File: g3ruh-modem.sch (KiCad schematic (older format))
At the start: 0 parts

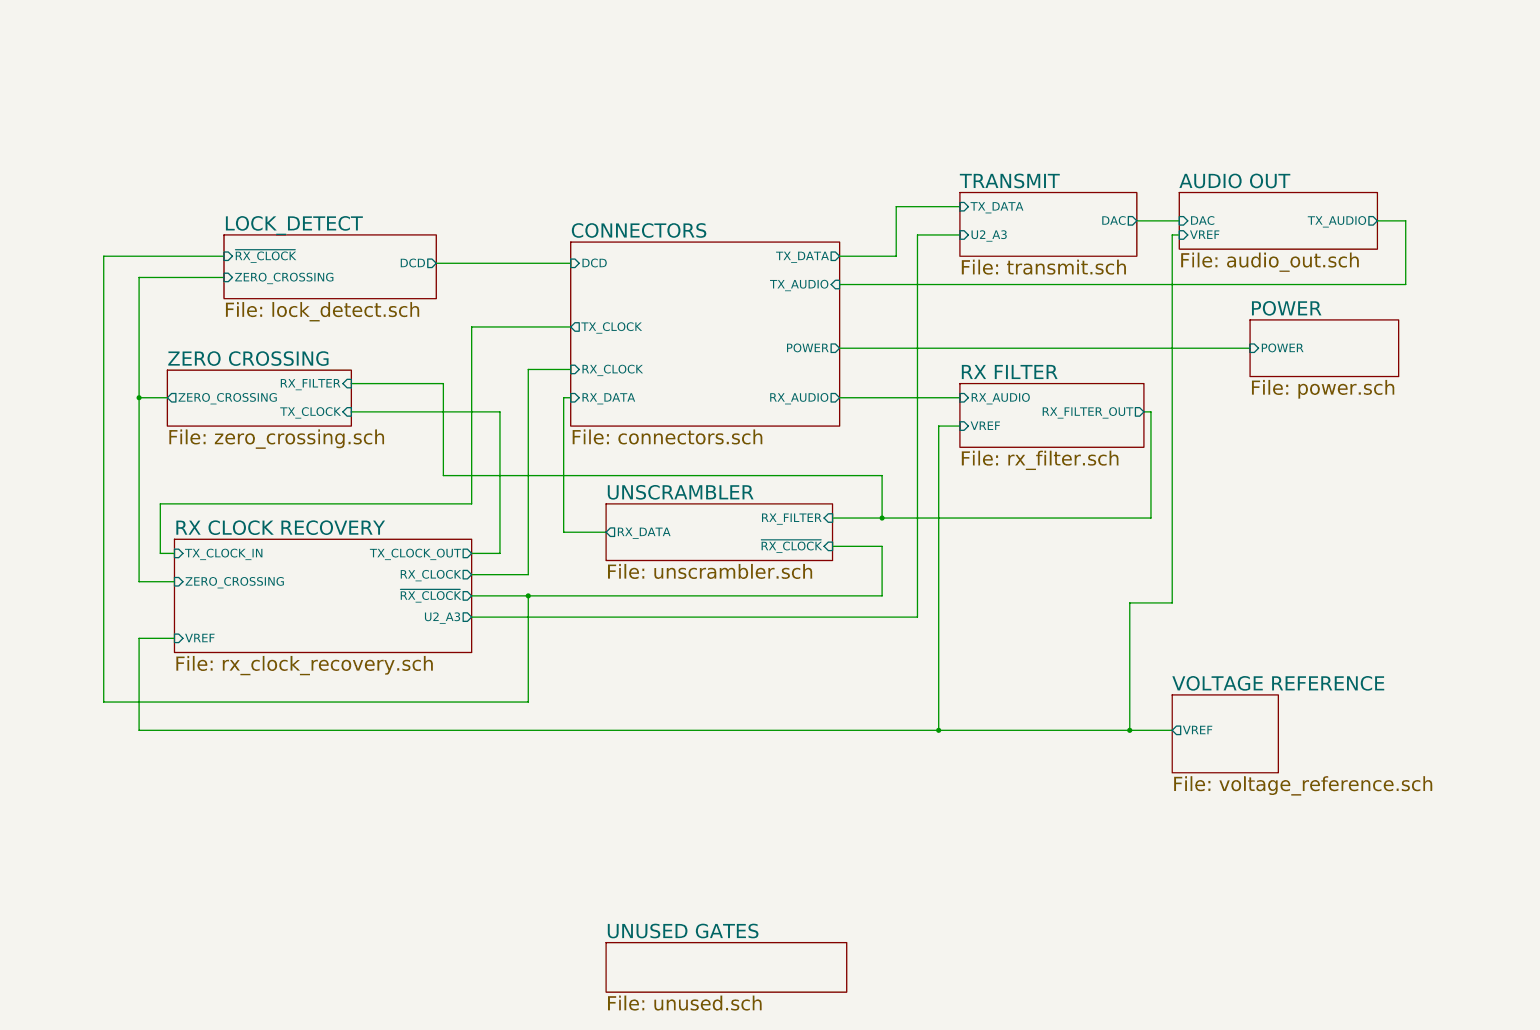
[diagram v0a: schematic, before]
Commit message: Rearrange blocks (hierarchical sheets) for better readability.
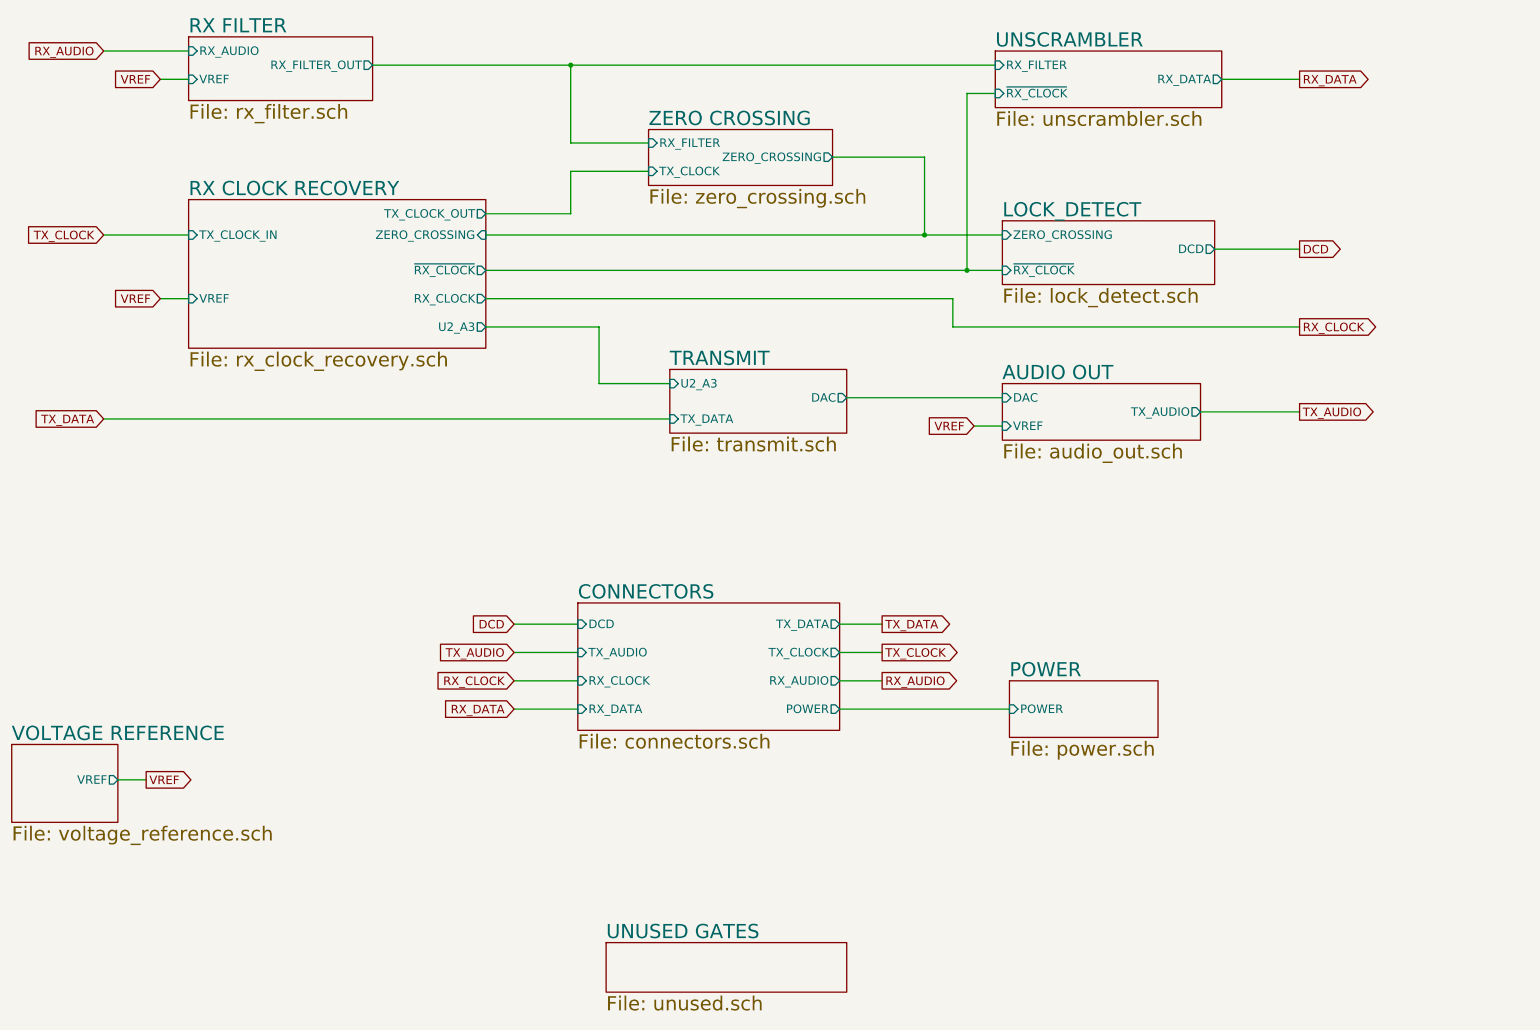
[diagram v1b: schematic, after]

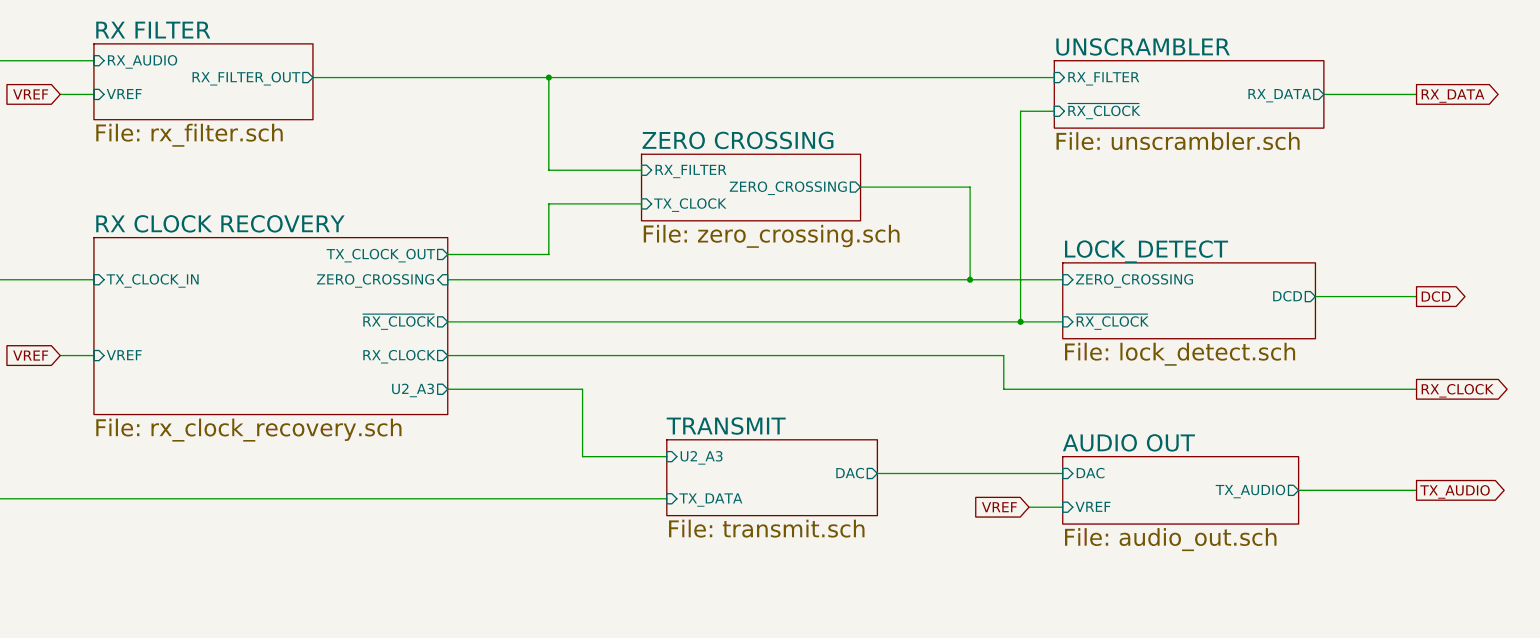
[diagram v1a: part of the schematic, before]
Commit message: Final parts placement and verified net against an actual Issue 3 board.
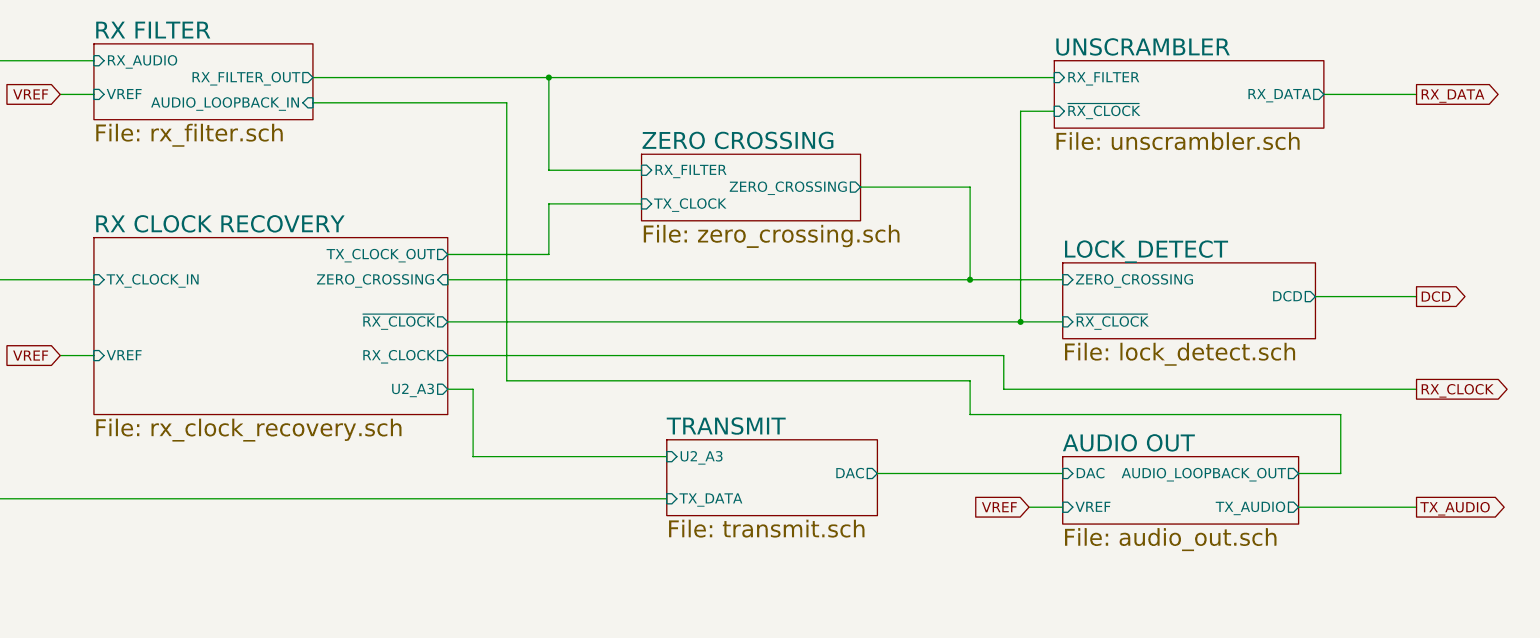
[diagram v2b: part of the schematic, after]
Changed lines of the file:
@@
 F3 "RX_AUDIO" I L 2150 900 60
 F4 "RX_FILTER_OUT" O R 3450 1000 60
+F5 "AUDIO_LOOPBACK_IN" I R 3450 1150 60
 $EndSheet
 $Sheet
@@
 F0 "AUDIO OUT" 100
 F1 "audio_out.sch" 100
-F2 "TX_AUDIO" O R 9300 3450 60
+F2 "TX_AUDIO" O R 9300 3550 60
 F3 "DAC" I L 7900 3350 60
 F4 "VREF" I L 7900 3550 60
+F5 "AUDIO_LOOPBACK_OUT" O R 9300 3350 60
 $EndSheet
 $Sheet
@@
 Text GLabel 10000 2300 2    60   Output ~ 0
 DCD
-Text GLabel 10000 3450 2    60   Output ~ 0
+Text GLabel 10000 3550 2    60   Output ~ 0
 TX_AUDIO
 Wire Wire Line
@@
 	10000 2300 9400 2300
 Wire Wire Line
-	10000 3450 9300 3450
+	10000 3550 9300 3550
 Text GLabel 10000 2850 2    60   Output ~ 0
 RX_CLOCK
@@
 	6800 3350 7900 3350
 Wire Wire Line
-	5550 3250 5050 3250
-Wire Wire Line
-	5050 3250 5050 2850
-Wire Wire Line
-	5050 2850 4250 2850
+	5550 3250 4400 3250
+Wire Wire Line
+	4400 3250 4400 2850
+Wire Wire Line
+	4400 2850 4250 2850
 Text GLabel 1550 900  0    60   Input ~ 0
 RX_AUDIO
@@
 Wire Wire Line
 	7700 3550 7900 3550
+Wire Wire Line
+	9300 3350 9550 3350
+Wire Wire Line
+	9550 3350 9550 3000
+Wire Wire Line
+	9550 3000 7350 3000
+Wire Wire Line
+	7350 3000 7350 2800
+Wire Wire Line
+	7350 2800 4600 2800
+Wire Wire Line
+	4600 2800 4600 1150
+Wire Wire Line
+	4600 1150 3450 1150
 $EndSCHEMATC
